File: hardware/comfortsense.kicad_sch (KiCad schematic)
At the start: 12 parts, among them J1 XIAO nRF52840 Sense (Left), J2 XIAO nRF52840 Sense (Right)

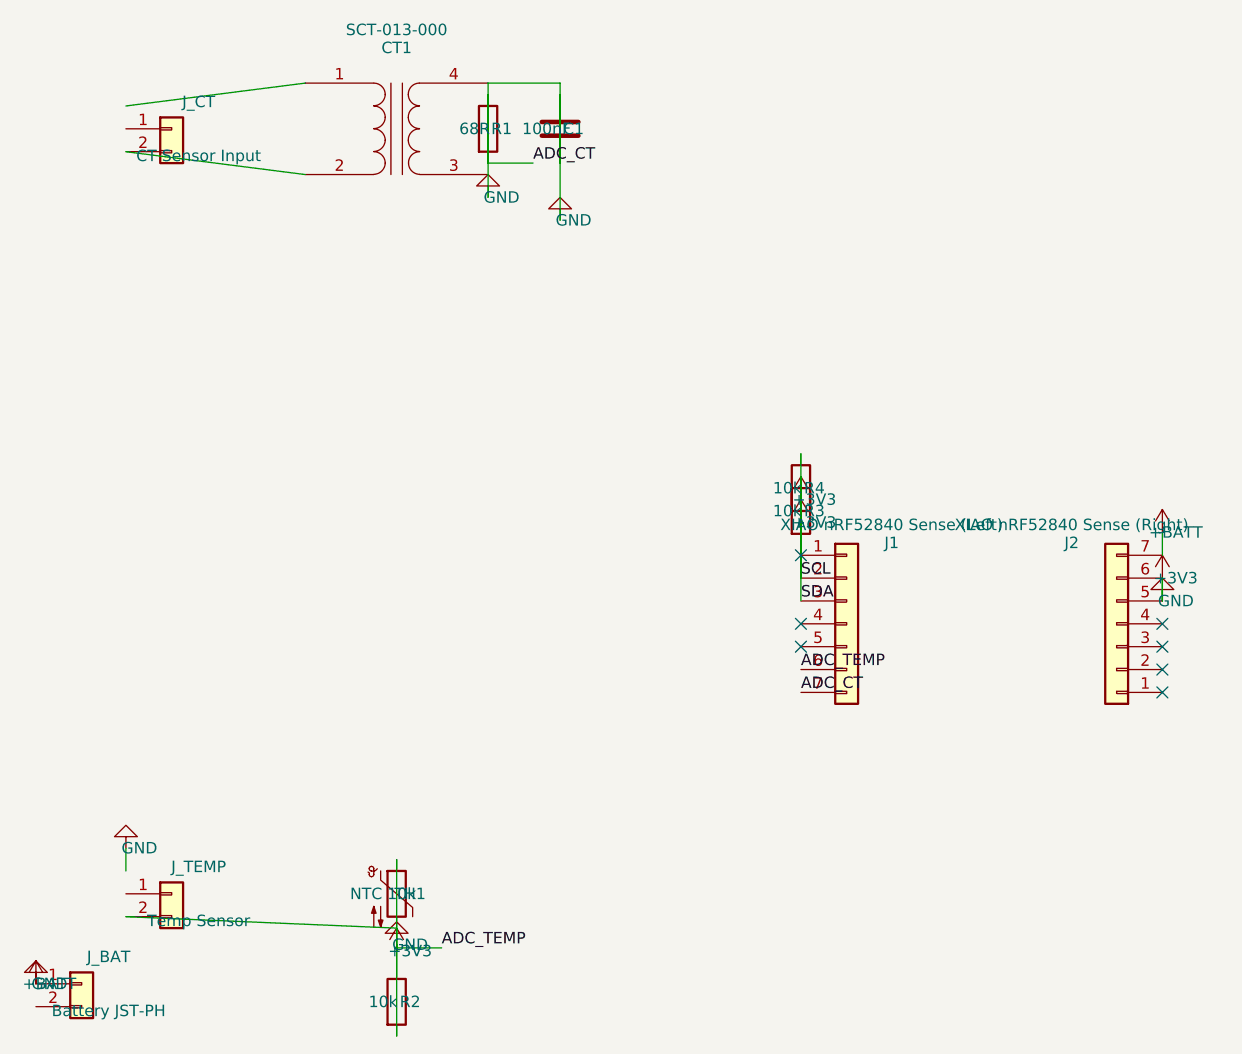
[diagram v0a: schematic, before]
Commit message: hw: schematic rev 0.2 — DS18B20 OneWire replaces NTC sub-circuit (Bill 6 / Case 9)
- J_DS18B20 3-pin connector + R_OW 4.7kΩ pull-up replace TH1 + R2 + J_TEMP
- Corrects pin assignment error: ADC_CT now on D2/P0.28, ONEWIRE on D3/P0.29
- gen_schematic.py updated; schematic regenerated at rev 0.2
- src/kicad_integration.py SIGNAL_TO_NET: outside_temp → ONEWIRE
- Case 9 recorded; Case 8 Condition 3 closed

Co-Authored-By: Claude Sonnet 4.6 <noreply@anthropic.com>
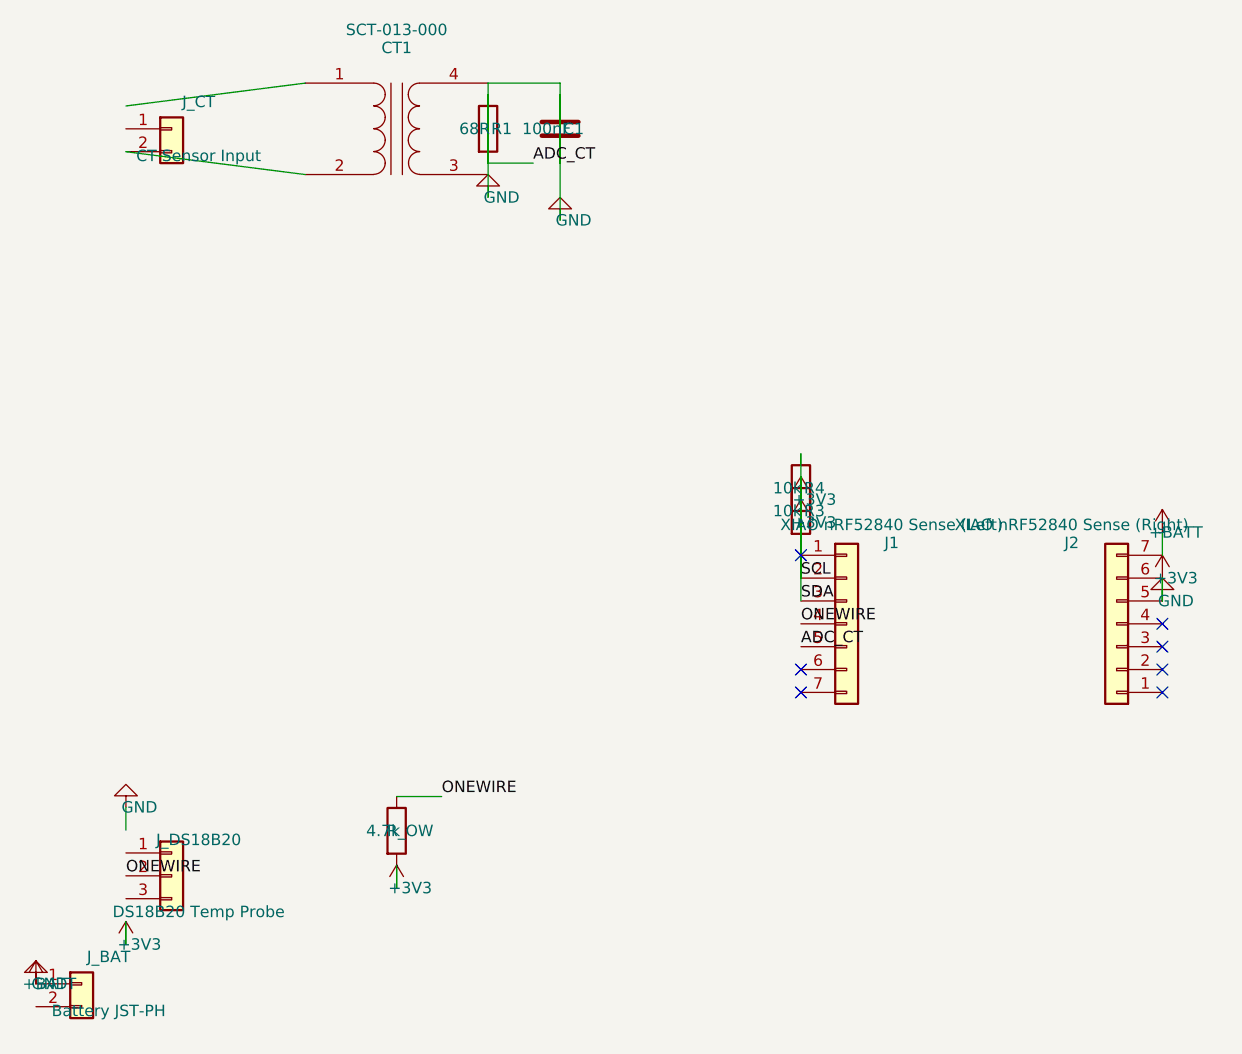
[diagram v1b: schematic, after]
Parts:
- removed J_TEMP: Temp Sensor, Connector_PinHeader_2.54mm:PinHeader_1x02_P2.54mm_Vertical, symbol Connector_Generic:Conn_01x02
- removed R2: 10k, Resistor_SMD:R_0402_1005Metric, symbol Device:R
- removed TH1: NTC 10k, Resistor_SMD:R_0402_1005Metric, symbol Device:Thermistor_NTC
- added J_DS18B20: DS18B20 Temp Probe, Connector_PinHeader_2.54mm:PinHeader_1x03_P2.54mm_Vertical, symbol Connector_Generic:Conn_01x03
- added R_OW: 4.7k, Resistor_SMD:R_0402_1005Metric, symbol Device:R
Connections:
- net +3V3: now also J1.5 (Pin_5), R_OW.2; no longer J1.7 (Pin_7)
- net ONEWIRE: now reaches J1.4 (Pin_4)
- net ONEWIRE: now also J_DS18B20.2 (Pin_2), R_OW.1
- net ADC_TEMP: no longer names the net of J1.6 (Pin_6)

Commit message: hw: fix schematic pin assignments and power connectivity
Fixes in scripts/gen_schematic.py:
- J1 (XIAO left): corrected pin_y index assignments — SCL on pin 6,
  SDA on pin 5, ADC_CT on pin 3, no_connects on pins 1/2/7 (D0,D1,TX)
- I2C pull-ups R3/R4: moved to (88,97)/(99,97) off J1 body; use net
  labels for signal end to avoid wired routing errors
- J_DS18B20 Conn_01x03: changed from ±5.08 offsets to direct power
  symbol placement at actual pin positions (±2.54); GND now correctly
  connects to pin 3 (was +3V3 due to wired distance mismatch)
- J_BAT: direct power symbol placement at pin positions (was floating)
- J2 (XIAO right): corrected pin_y2 array direction for rot=180;
  direct power symbol placement at actual pin positions

Netlist now shows: GND net exists, +BATT net exists, J_DS18B20 pin3→GND,
J2 pin1→+BATT, J2 pin2→GND, J2 pin3→+3V3, J1 pins→correct nets.

Co-Authored-By: Claude Sonnet 4.6 <noreply@anthropic.com>
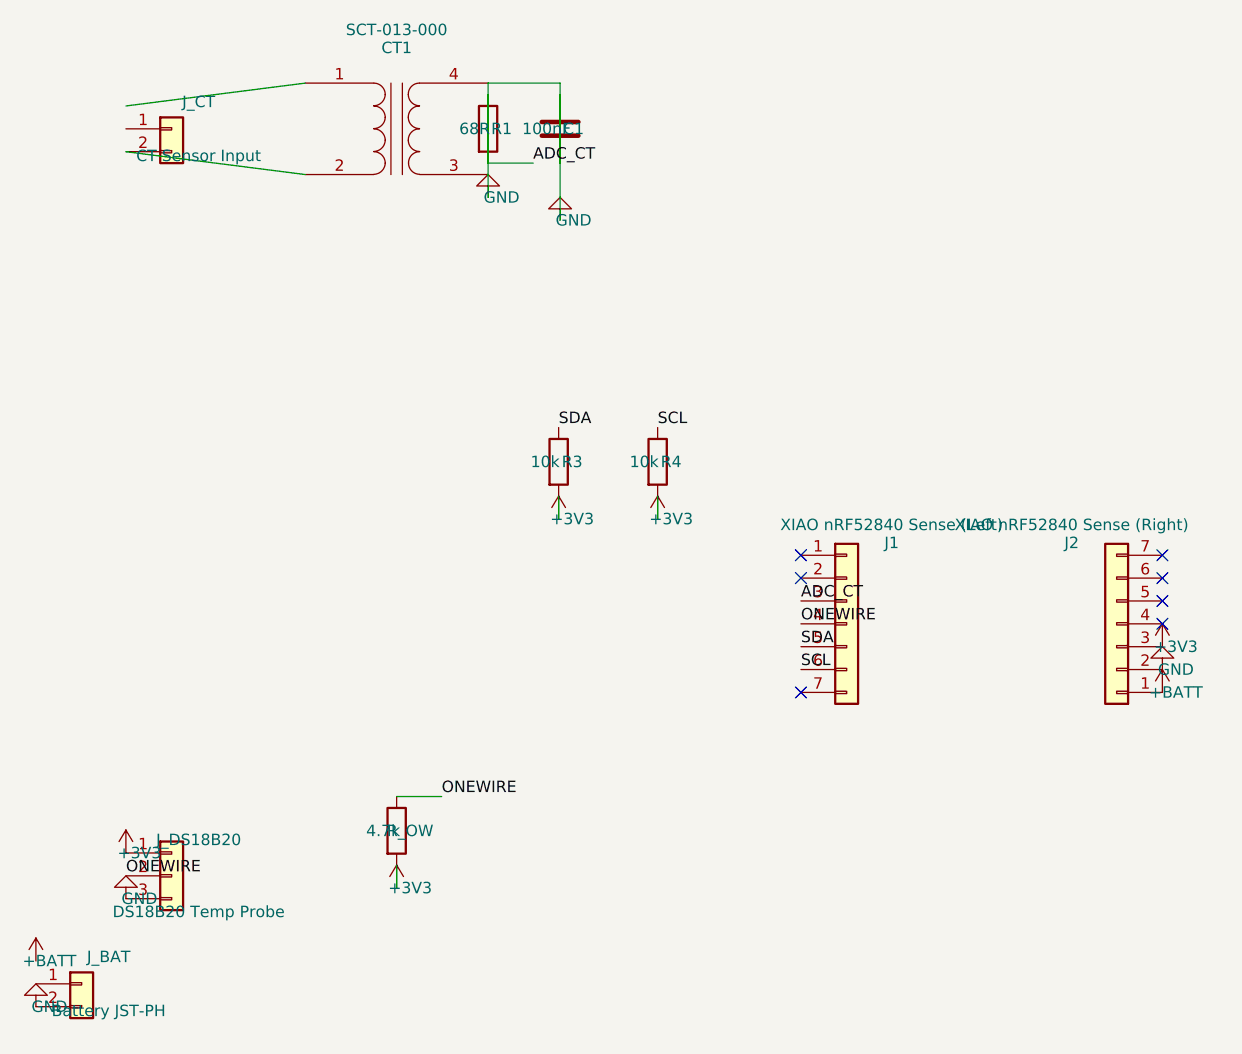
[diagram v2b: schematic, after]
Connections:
- net +3V3: now also J2.3 (Pin_3), J_DS18B20.1 (Pin_1); no longer C1.1, C1.2, CT1.3 (SA), CT1.4 (SB), J1.2 (Pin_2), J1.3 (Pin_3), J1.5 (Pin_5), J2.5 (Pin_5), J2.6 (Pin_6), J2.7 (Pin_7), J_BAT.1 (Pin_1), R1.1, R1.2, R3.1, R4.1
- net SCL: now reaches J1.6 (Pin_6)
- net SCL: now also R4.1
- net GND: now reaches J_BAT.2 (Pin_2)
- net GND: now also C1.1, C1.2, CT1.3 (SA), CT1.4 (SB), J1.3 (Pin_3), J2.2 (Pin_2), J_DS18B20.3 (Pin_3), R1.1, R1.2
- net +BATT: now reaches J2.1 (Pin_1)
- new net SDA: J1.5 (Pin_5), R3.1
